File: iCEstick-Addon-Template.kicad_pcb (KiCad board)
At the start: 2 copper layers, 26.7 x 27.9 mm, 3 parts, among them J1 Conn_01x10, J2 PMOD, J3 Conn_01x10

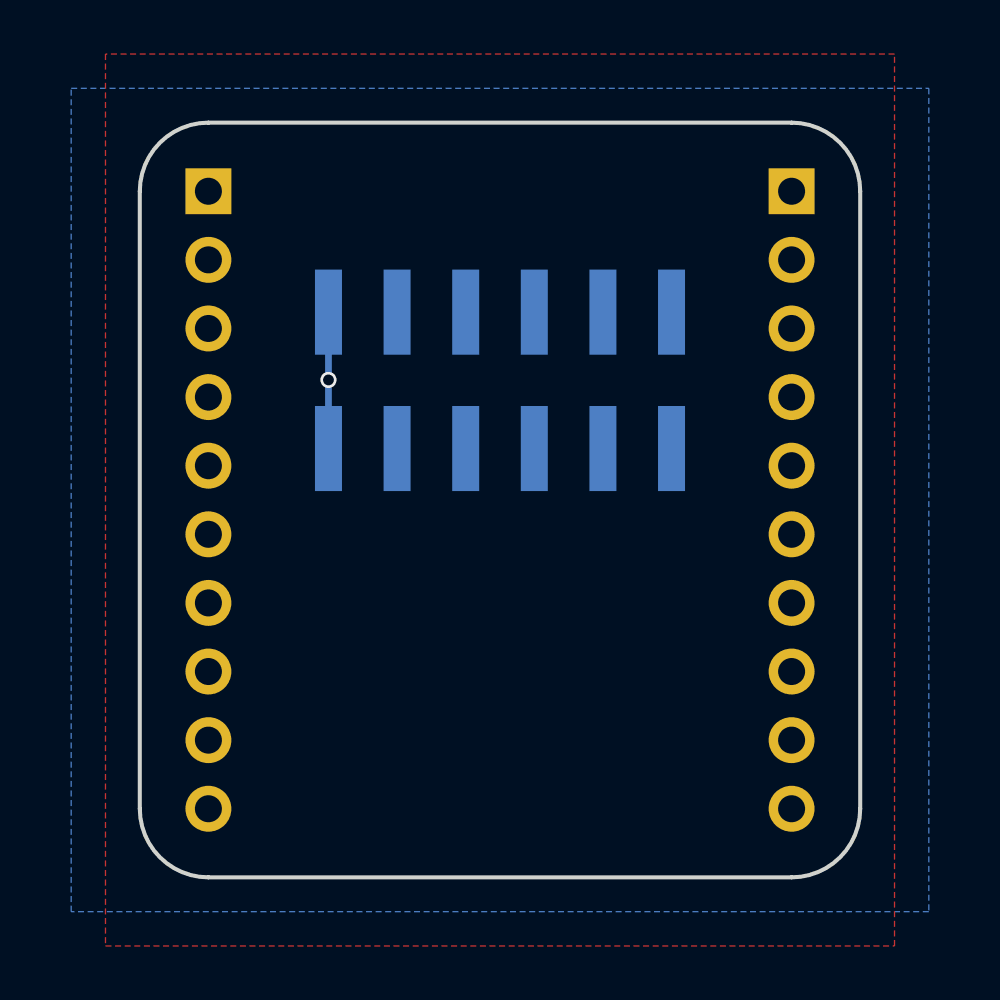
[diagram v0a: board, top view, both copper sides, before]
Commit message: made pin headers smd; removed 3v3 plane
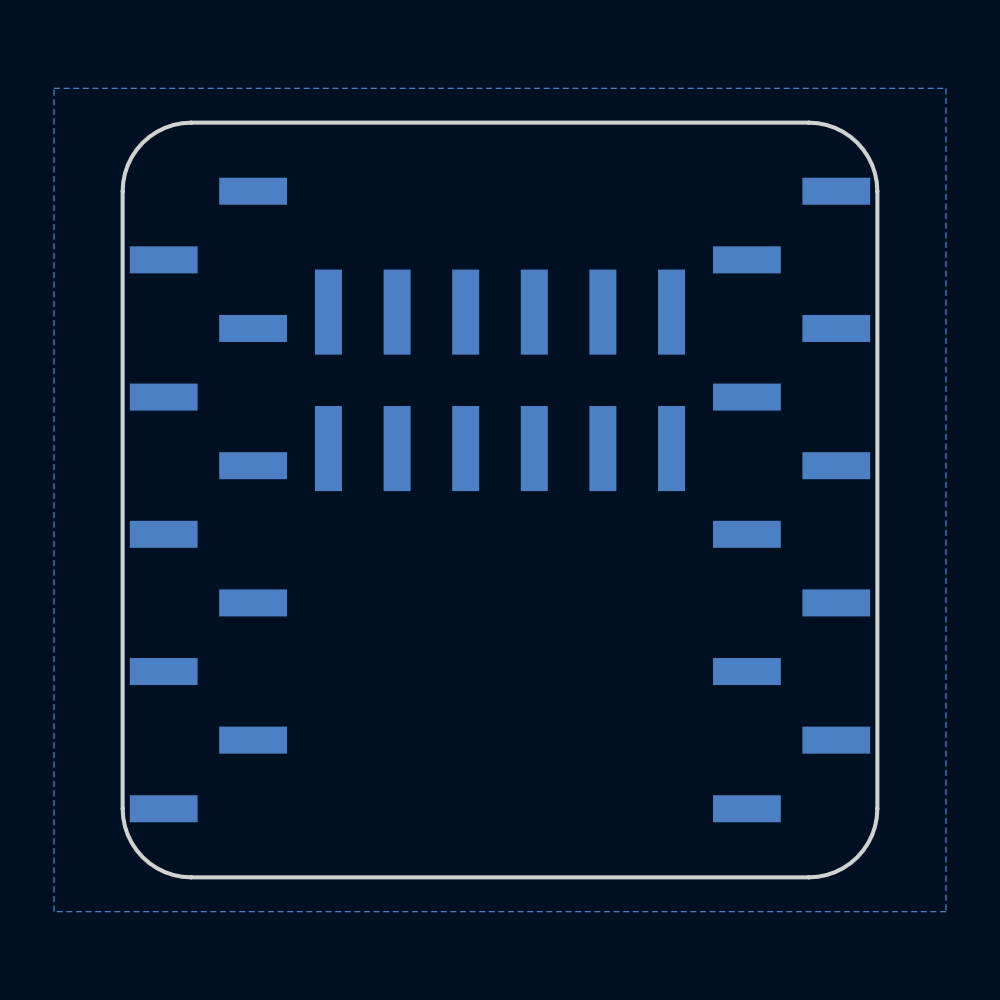
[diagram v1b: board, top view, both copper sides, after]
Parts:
- J1, J3: footprint Pin_Headers:Pin_Header_Straight_1x10_Pitch2.54mm -> Pin_Headers:Pin_Header_Straight_1x10_Pitch2.54mm_SMD_Pin1Left
- moved J1 11.4 mm to (116.2, 102.9)
- moved J3 11.4 mm to (137.8, 102.9)
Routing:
- net +3V3: track 5.05 -> 0.00 mm, vias 1 -> 0
- removed copper zone on F.Cu, net +3V3
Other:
- board size 26.7 x 27.9 mm -> 27.9 x 27.9 mm
